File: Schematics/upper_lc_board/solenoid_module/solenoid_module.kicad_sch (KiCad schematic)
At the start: 16 parts

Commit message: reviewing schematics
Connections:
- net SOL2_RET: now also D?.1 (K); no longer D?.2 (A)
- net at R?.1: now also D?.2 (A); no longer D?.1 (K)
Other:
- moved on the sheet: D?, R?
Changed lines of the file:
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@@
-	(wire
-		(pts
-			(xy 101.6 140.97) (xy 99.06 140.97)
-		)
-		(stroke
-			(width 0)
-			(type default)
-		)
-	)
 	(wire
 		(pts
@@
 	(global_label "SOL1_RET"
 		(shape input)
-		(at 91.44 140.97 180)
+		(at 91.44 142.24 180)
 		(fields_autoplaced yes)
 		(effects
@@
 		)
 		(property "Intersheetrefs" "${INTERSHEET_REFS}"
-			(at 79.323 140.97 0)
+			(at 79.323 142.24 0)
 			(effects
 				(font
@@
 	(global_label "SOL2_RET"
 		(shape input)
-		(at 92.71 124.46 180)
+		(at 91.44 125.73 180)
 		(fields_autoplaced yes)
 		(effects
@@
 		)
 		(property "Intersheetrefs" "${INTERSHEET_REFS}"
-			(at 80.593 124.46 0)
+			(at 79.323 125.73 0)
 			(effects
 				(font
@@
 	(symbol
 		(lib_id "Device:LED")
-		(at 96.52 124.46 180)
+		(at 95.25 125.73 0)
 		(unit 1)
 		(exclude_from_sim no)
@@
 		(dnp no)
 		(property "Reference" "D?"
-			(at 96.52 129.54 0)
+			(at 95.25 120.65 0)
 			(effects
 				(font
@@
 		)
 		(property "Value" "SOL_LED"
-			(at 96.52 127.254 0)
+			(at 95.25 122.936 0)
 			(effects
 				(font
@@
 		)
 		(property "Footprint" "LED_SMD:LED_0805_2012Metric"
-			(at 96.52 124.46 0)
+			(at 95.25 125.73 0)
 			(effects
 				(font
@@
 		)
 		(property "Datasheet" "~"
-			(at 96.52 124.46 0)
+			(at 95.25 125.73 0)
 			(effects
 				(font
@@
 		)
 		(property "Description" "Light emitting diode"
-			(at 96.52 124.46 0)
+			(at 95.25 125.73 0)
 			(effects
 				(font
@@
 	(symbol
 		(lib_id "power:+24V")
-		(at 107.95 124.46 270)
+		(at 106.68 125.73 270)
 		(unit 1)
 		(exclude_from_sim no)
@@
 		(fields_autoplaced yes)
 		(property "Reference" "#PWR?"
-			(at 104.14 124.46 0)
+			(at 102.87 125.73 0)
 			(effects
 				(font
@@
 		)
 		(property "Value" "+24V"
-			(at 111.76 124.4601 90)
+			(at 110.49 125.7301 90)
 			(effects
 				(font
@@
 		)
 		(property "Footprint" ""
-			(at 107.95 124.46 0)
+			(at 106.68 125.73 0)
 			(effects
 				(font
@@
 		)
 		(property "Datasheet" ""
-			(at 107.95 124.46 0)
+			(at 106.68 125.73 0)
 			(effects
 				(font
@@
 		)
 		(property "Description" "Power symbol creates a global label with name \"+24V\""
-			(at 107.95 124.46 0)
+			(at 106.68 125.73 0)
 			(effects
 				(font
@@
 	(symbol
 		(lib_id "Device:R")
-		(at 105.41 140.97 90)
+		(at 102.87 142.24 90)
 		(unit 1)
 		(exclude_from_sim no)
@@
 		(dnp no)
 		(property "Reference" "R?"
-			(at 105.156 134.874 90)
+			(at 102.616 136.144 90)
 			(effects
 				(font
@@
 		)
 		(property "Value" "2.2k"
-			(at 105.156 137.16 90)
+			(at 102.616 138.43 90)
 			(effects
 				(font
@@
 		)
 		(property "Footprint" "Resistor_SMD:R_1210_3225Metric"
-			(at 105.41 142.748 90)
+			(at 102.87 144.018 90)
 			(effects
 				(font
@@
 		)
 		(property "Datasheet" "~"
-			(at 105.41 140.97 0)
+			(at 102.87 142.24 0)
 			(effects
 				(font
@@
 		)
 		(property "Description" "Current Limiting Resistor"
-			(at 105.41 140.97 0)
+			(at 102.87 142.24 0)
 			(effects
 				(font
@@
 	(symbol
 		(lib_id "power:+24V")
-		(at 109.22 140.97 270)
+		(at 106.68 142.24 270)
 		(unit 1)
 		(exclude_from_sim no)
@@
 		(fields_autoplaced yes)
 		(property "Reference" "#PWR?"
-			(at 105.41 140.97 0)
+			(at 102.87 142.24 0)
 			(effects
 				(font
@@
 		)
 		(property "Value" "+24V"
-			(at 113.03 140.9701 90)
+			(at 110.49 142.2401 90)
 			(effects
 				(font
@@
 		)
 		(property "Footprint" ""
-			(at 109.22 140.97 0)
+			(at 106.68 142.24 0)
 			(effects
 				(font
@@
 		)
 		(property "Datasheet" ""
-			(at 109.22 140.97 0)
+			(at 106.68 142.24 0)
 			(effects
 				(font
@@
 		)
 		(property "Description" "Power symbol creates a global label with name \"+24V\""
-			(at 109.22 140.97 0)
+			(at 106.68 142.24 0)
 			(effects
 				(font
@@
 	(symbol
 		(lib_id "Device:R")
-		(at 104.14 124.46 90)
+		(at 102.87 125.73 90)
 		(unit 1)
 		(exclude_from_sim no)
@@
 		(dnp no)
 		(property "Reference" "R?"
-			(at 104.14 119.888 90)
+			(at 102.87 121.158 90)
 			(effects
 				(font
@@
 		)
 		(property "Value" "2.2k"
-			(at 104.14 121.92 90)
+			(at 102.87 123.19 90)
 			(effects
 				(font
@@
 		)
 		(property "Footprint" "Resistor_SMD:R_1210_3225Metric"
-			(at 104.14 126.238 90)
+			(at 102.87 127.508 90)
 			(effects
 				(font
@@
 		)
 		(property "Datasheet" "~"
-			(at 104.14 124.46 0)
+			(at 102.87 125.73 0)
 			(effects
 				(font
@@
 		)
 		(property "Description" "Current Limiting Resistor"
-			(at 104.14 124.46 0)
+			(at 102.87 125.73 0)
 			(effects
 				(font
@@
 	(symbol
 		(lib_id "Device:LED")
-		(at 95.25 140.97 0)
+		(at 95.25 142.24 0)
 		(unit 1)
 		(exclude_from_sim no)
@@
 		(dnp no)
 		(property "Reference" "D?"
-			(at 93.472 135.128 0)
+			(at 93.472 136.398 0)
 			(effects
 				(font
@@
 		)
 		(property "Value" "SOL_LED"
-			(at 93.472 137.16 0)
+			(at 93.472 138.43 0)
 			(effects
 				(font
@@
 		)
 		(property "Footprint" "LED_SMD:LED_0805_2012Metric"
-			(at 95.25 140.97 0)
+			(at 95.25 142.24 0)
 			(effects
 				(font
@@
 		)
 		(property "Datasheet" "~"
-			(at 95.25 140.97 0)
+			(at 95.25 142.24 0)
 			(effects
 				(font
@@
 		)
 		(property "Description" "Light emitting diode"
-			(at 95.25 140.97 0)
-			(effects
-				(font
+			(at 95.25 142.24 0)
+			(effects
+				(font

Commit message: temp commit for layout work
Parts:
- F1: footprint (none) -> 0679L0250-05:FUSC6125X279N
- R? (x3): footprint Capacitor_SMD:C_0402_1005Metric -> Resistor_SMD:R_0402_1005Metric
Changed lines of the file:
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@@
 			)
 		)
-		(property "Footprint" "Capacitor_SMD:C_0402_1005Metric"
+		(property "Footprint" "Resistor_SMD:R_0402_1005Metric"
 			(at 168.91 88.392 90)
 			(effects
@@
 			)
 		)
-		(property "Footprint" "Capacitor_SMD:C_0402_1005Metric"
+		(property "Footprint" "Resistor_SMD:R_0402_1005Metric"
 			(at 182.118 137.16 90)
 			(effects
@@
 			)
 		)
-		(property "Footprint" "Capacitor_SMD:C_0402_1005Metric"
+		(property "Footprint" "Resistor_SMD:R_0402_1005Metric"
 			(at 168.91 131.572 90)
 			(effects
@@
 			)
 		)
-		(property "Footprint" ""
+		(property "Footprint" "0679L0250-05:FUSC6125X279N"
 			(at 98.552 49.53 90)
 			(effects

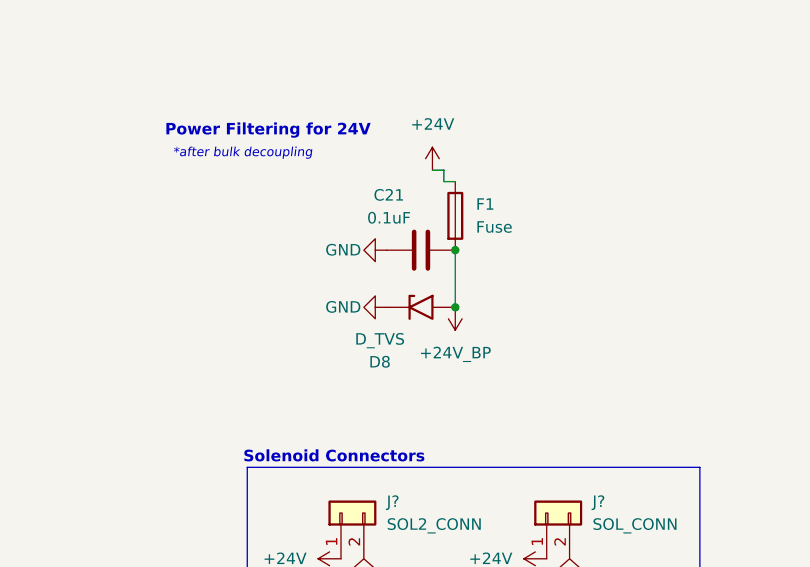
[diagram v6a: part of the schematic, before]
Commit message: update schematic & board with smaller diode footprints
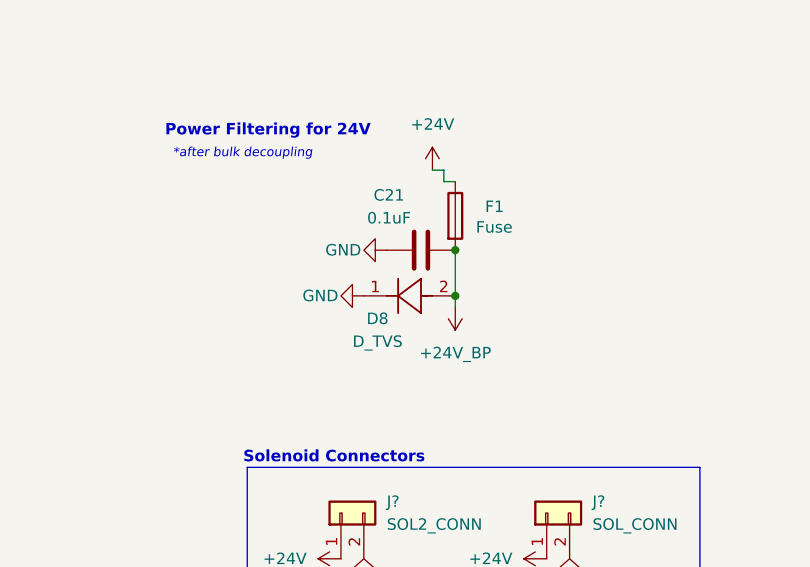
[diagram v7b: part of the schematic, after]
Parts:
- D8: footprint SMBJ28A:DIOM5436X244N -> SMA6L30A:SMASeries_LTF-L; symbol Diode:1.5KExxA -> SMA6L30A:SMA6L30A
- D? (x2): footprint SK44BL-TP:DIOM4336X265N -> D_FB_SDM4A:SDM4A40EP37B
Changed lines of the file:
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@@
 	)
 	(junction
-		(at 100.33 59.69)
+		(at 100.33 58.42)
 		(diameter 0)
 		(color 132 0 0 1)
@@
 	(wire
 		(pts
-			(xy 204.47 87.63) (xy 204.47 90.17)
-		)
-		(stroke
-			(width 0)
-			(type default)
-		)
-	)
-	(wire
-		(pts
-			(xy 99.06 45.72) (xy 99.06 44.45)
-		)
-		(stroke
-			(width 0)
-			(type default)
-		)
-	)
-	(wire
-		(pts
-			(xy 172.72 133.35) (xy 180.34 133.35)
-		)
-		(stroke
-			(width 0)
-			(type default)
-		)
-	)
-	(wire
-		(pts
-			(xy 203.2 90.17) (xy 204.47 90.17)
-		)
-		(stroke
-			(width 0)
-			(type default)
-		)
-	)
-	(wire
-		(pts
-			(xy 100.33 53.34) (xy 100.33 59.69)
+			(xy 100.33 58.42) (xy 100.33 59.69)
 		)
 		(stroke
@@
 			(type default)
 			(color 194 0 0 1)
+		)
+	)
+	(wire
+		(pts
+			(xy 100.33 53.34) (xy 100.33 58.42)
+		)
+		(stroke
+			(width 0)
+			(type default)
+			(color 194 0 0 1)
+		)
+	)
+	(wire
+		(pts
+			(xy 204.47 87.63) (xy 204.47 90.17)
+		)
+		(stroke
+			(width 0)
+			(type default)
+		)
+	)
+	(wire
+		(pts
+			(xy 99.06 45.72) (xy 99.06 44.45)
+		)
+		(stroke
+			(width 0)
+			(type default)
+		)
+	)
+	(wire
+		(pts
+			(xy 172.72 133.35) (xy 180.34 133.35)
+		)
+		(stroke
+			(width 0)
+			(type default)
+		)
+	)
+	(wire
+		(pts
+			(xy 203.2 90.17) (xy 204.47 90.17)
+		)
+		(stroke
+			(width 0)
+			(type default)
 		)
 	)
@@
 	(symbol
 		(lib_id "power:GND")
-		(at 92.71 59.69 270)
+		(at 90.17 58.42 270)
 		(unit 1)
 		(exclude_from_sim no)
@@
 		(dnp no)
 		(property "Reference" "#PWR081"
-			(at 86.36 59.69 0)
+			(at 83.82 58.42 0)
 			(effects
 				(font
@@
 		)
 		(property "Value" "GND"
-			(at 87.884 59.69 90)
+			(at 85.344 58.42 90)
 			(effects
 				(font
@@
 		)
 		(property "Footprint" ""
-			(at 92.71 59.69 0)
+			(at 90.17 58.42 0)
 			(effects
 				(font
@@
 		)
 		(property "Datasheet" ""
-			(at 92.71 59.69 0)
+			(at 90.17 58.42 0)
 			(effects
 				(font
@@
 		)
 		(property "Description" "Power symbol creates a global label with name \"GND\" , ground"
-			(at 92.71 59.69 0)
+			(at 90.17 58.42 0)
 			(effects
 				(font
@@
 			)
 		)
-		(property "Footprint" "SK44BL-TP:DIOM4336X265N"
+		(property "Footprint" "D_FB_SDM4A:SDM4A40EP37B"
 			(at 189.23 121.92 0)
 			(effects
@@
 			)
 		)
-		(property "Datasheet" "https://www.mccsemi.com/pdf/Products/SK42BL-SK44BL(DO-214AA).pdf"
+		(property "Datasheet" "https://www.diodes.com/assets/Datasheets/SDM4A40EP3.pdf"
 			(at 189.23 121.92 0)
 			(effects
@@
 		(dnp no)
 		(property "Reference" "F1"
-			(at 102.616 48.26 0)
+			(at 103.632 48.514 0)
 			(effects
 				(font
@@
 	)
 	(symbol
-		(lib_id "Diode:1.5KExxA")
-		(at 96.52 59.69 0)
+		(lib_id "SMA6L30A:SMA6L30A")
+		(at 100.33 58.42 180)
 		(unit 1)
 		(exclude_from_sim no)
@@
 		(dnp no)
 		(property "Reference" "D8"
-			(at 91.948 65.786 0)
+			(at 91.694 60.96 0)
 			(effects
 				(font
@@
 		)
 		(property "Value" "D_TVS"
-			(at 91.948 63.246 0)
-			(effects
-				(font
-					(size 1.27 1.27)
-				)
-			)
-		)
-		(property "Footprint" "SMBJ28A:DIOM5436X244N"
-			(at 96.52 64.77 0)
-			(effects
-				(font
-					(size 1.27 1.27)
-				)
-				(hide yes)
-			)
-		)
-		(property "Datasheet" "https://www.littelfuse.com/assetdocs/tvs-diodes-smbj-series-datasheet?assetguid=ba555e99-a12d-4f72-a0b6-86b06c67171e"
-			(at 95.25 59.69 0)
-			(effects
-				(font
-					(size 1.27 1.27)
+			(at 91.694 63.5 0)
+			(effects
+				(font
+					(size 1.27 1.27)
+				)
+			)
+		)
+		(property "Footprint" "SMA6L30A:SMASeries_LTF-L"
+			(at 100.33 58.42 0)
+			(effects
+				(font
+					(size 1.27 1.27)
+					(italic yes)
+				)
+				(hide yes)
+			)
+		)
+		(property "Datasheet" "SMA6L30A"
+			(at 100.33 58.42 0)
+			(effects
+				(font
+					(size 1.27 1.27)
+					(italic yes)
 				)
 				(hide yes)
@@
 		)
 		(property "Description" "TVS Diode"
-			(at 96.52 59.69 0)
+			(at 100.33 58.42 0)
 			(effects
 				(font
@@
 			)
 		)
-		(property "Footprint" "SK44BL-TP:DIOM4336X265N"
+		(property "Footprint" "D_FB_SDM4A:SDM4A40EP37B"
 			(at 204.47 83.82 0)
 			(effects
@@
 			)
 		)
-		(property "Datasheet" "https://www.mccsemi.com/pdf/Products/SK42BL-SK44BL(DO-214AA).pdf"
+		(property "Datasheet" "https://www.diodes.com/assets/Datasheets/SDM4A40EP3.pdf"
 			(at 204.47 83.82 0)
 			(effects

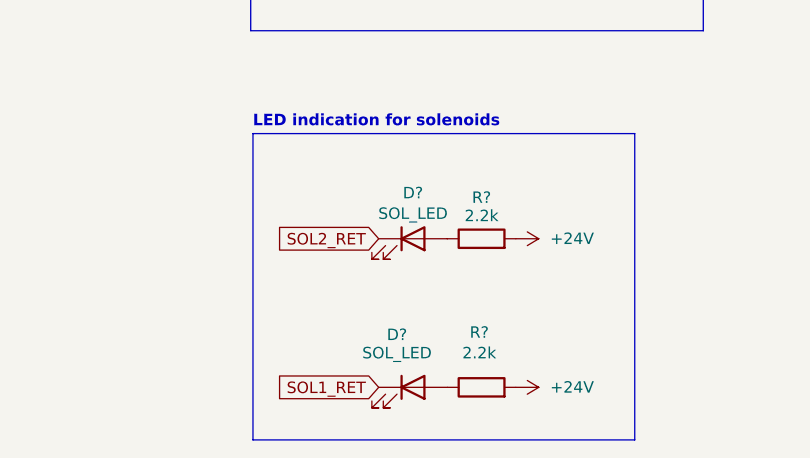
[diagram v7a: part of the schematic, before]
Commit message: fix footprint designators
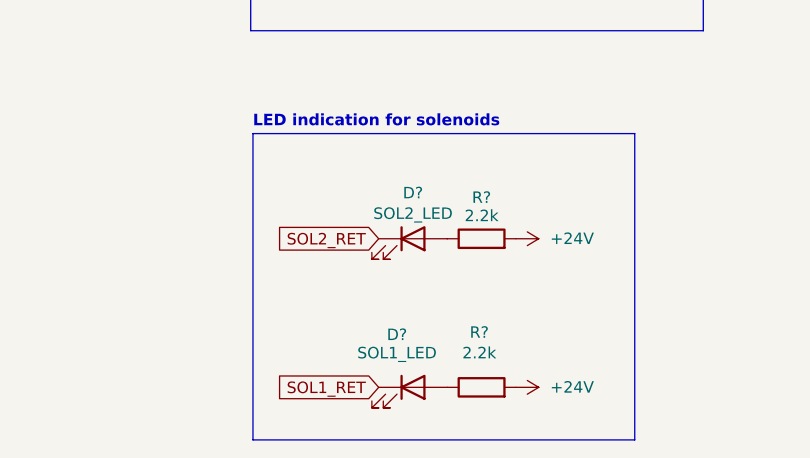
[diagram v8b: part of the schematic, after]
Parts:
- D?: value SOL_LED -> SOL2_LED
- D?: value SOL_LED -> SOL1_LED
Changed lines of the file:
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@@
 			)
 		)
-		(property "Value" "SOL_LED"
+		(property "Value" "SOL2_LED"
 			(at 95.25 122.936 0)
 			(effects
@@
 			)
 		)
-		(property "Value" "SOL_LED"
+		(property "Value" "SOL1_LED"
 			(at 93.472 138.43 0)
 			(effects
